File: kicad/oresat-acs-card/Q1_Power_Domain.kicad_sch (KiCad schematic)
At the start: 69 parts, among them Q11 MOSFET-PCH-SOT23-6, Q12 MOSFET-PCH-SOT23-6, Q13 PMV45EN2R, Q14 PMV45EN2R, Q15 MOSFET-PCH-dual-SOT23-6, U10 MAX4211FETE, U11 MIC842LYC5-TR, U12 MIC842LYC5-TR, U9 MAX7310ATE

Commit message: Updated ACS board. Changed mezzanine pinouts. Added 5 V supplies for each quadrant. Updated layout.
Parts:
- added C20: 10u, oresat-acs-card:.0805-B-NOSILK, symbol Device:C_Small
- added C57: 1u, Resistor_SMD:R_0603_1608Metric, symbol Device:C_Small
- added C64: 22u, Capacitor_SMD:C_1210_3225Metric, symbol Device:C_Small
- added C84: CL10B104KB8NNNL, oresat-acs-card:.0603-C-NOSILK, symbol oresat-acs-card-eagle-import:C-EU0603-C-NOSILK
- added D1: 150060VS55040, oresat-acs-card:LED-0603, symbol oresat-live-card-eagle-import:LED-GREEN0603
- added L1: 6.8u, oresat-acs-card:ECS-MPI4040, symbol oresat-live-card-eagle-import:L-ECS-MPI4040
- added R116, R117: RC0603FR-0710KL, oresat-acs-card:.0603-C-NOSILK, symbol oresat-acs-card-eagle-import:R-US_0603-C-NOSILK
- added R14, R26: 10k, Resistor_SMD:R_0603_1608Metric, symbol oresat-live-card-eagle-import:R-US_0603-A
- added TP51: TEST-POINT-LARGE-SQUARE, oresat-acs-card:1X01, symbol oresat-acs-card-eagle-import:TEST-POINT-LARGE-SQUARE
- added U24: TPS62112, oresat-acs-card:S-PVQFN-16, symbol oresat-live-card-eagle-import:TPS6211X
- added U38: TS5A21366DCUR, oresat-acs-card:DCU-R-PDSO-G8, symbol oresat-acs-card-eagle-import:TS5A21366DCUR
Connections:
- net GND: now also C20.2, C57.2, C64.2, C84.1, D1.C, U24.1 (GND), U24.11 (GND), U24.12 (GND), U24.16 (GND), U24.6 (LBO), U24.7 (LBI), U24.9 (GND), U24.PAD (GND), U38.4 (GND)
- net VBUSP_Q1: now also C20.1, C57.1, R14.2, U24.2 (VIN), U24.3 (VIN), U24.4 (EN), U24.8 (VIN)
- net VPD_Q1: now also C84.2, U38.8 (VCC)
- net at TP39.1, U9.12 (IO7): now also U38.3 (IN2), U38.7 (IN1)
- new net: D1.A, R26.1
- new net: R116.2, U38.1 (NO1)
- new net: R117.2, U38.5 (NO2)
- new net: R14.1, U24.5 (SYNC)
- new net: L1.1, U24.14 (SW), U24.15 (SW)
- new net 5V_Q1: C64.1, L1.2, R26.2, TP51.1, U24.10 (FB)
- new net C3-UART-RX: R116.1
- new net C3-UART-TX: R117.1
- new net UART_RX_Q1: U38.6 (COM2)
- new net UART_TX_Q1: U38.2 (COM1)
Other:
- note added: "0805"
- note added: "5V Card Switching Supply"

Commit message: Updated 5 V regulator and tweaked card layout. Cleaned up silkscreen layer and schematic.
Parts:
- removed L1: 6.8u, oresat-acs-card:ECS-MPI4040, symbol oresat-live-card-eagle-import:L-ECS-MPI4040
- removed R14, R26: 10k, Resistor_SMD:R_0603_1608Metric, symbol oresat-live-card-eagle-import:R-US_0603-A
- removed U24: TPS62112, oresat-acs-card:S-PVQFN-16, symbol oresat-live-card-eagle-import:TPS6211X
- added L1: 3u3, Inductor_SMD:L_Coilcraft_XxL4030, symbol Device:L_Small
- added R14, R19, R26: 100k, Resistor_SMD:R_0603_1608Metric, symbol Device:R_Small_US
- added U24: LTC3624, Package_DFN_QFN:DFN-8-1EP_3x3mm_P0.5mm_EP1.65x2.38mm, symbol U-Linear Tech-LTC3624:LTC3624
- C20: footprint oresat-acs-card:.0805-B-NOSILK -> Capacitor_SMD:C_0805_2012Metric; Distributor DigiKey -> (none); MPN CGA4J1X7R0J106M125AC -> (none)
- C57: value 1u -> 2u2; footprint Resistor_SMD:R_0603_1608Metric -> Capacitor_SMD:C_0603_1608Metric; Distributor DigiKey -> (none); MPN CGA3E1X7R1E105M080AE -> (none)
- C64: value 22u -> 47u; footprint Capacitor_SMD:C_1210_3225Metric -> Capacitor_SMD:C_1206_3216Metric; Distributor DigiKey -> (none); MFR (none) -> KYOCERA AVX; MPN CGA6P1X7R1C226M250AC -> 1206YD476MAT2A
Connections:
- net 5V_Q1: now also L1.2, R26.1, U24.5 (FB)
- net GND: now also R19.2, U24.8 (GND), U24.9 (GND)
- net VBUSP_Q1: now also U24.2 (Vin), U24.3 (RUN); no longer C57.1
- net at D1.A: now also R26.2
- new net: C57.1, R14.2, U24.6 (INTVcc)
- new net: L1.1, U24.1 (SW)
- new net: R14.1, R19.1, U24.7 (MODE)
- no-connect marks 0 -> 1
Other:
- note removed: "0805"
- moved on the sheet: C11, C12, C13, C14, C15, C84, D1, D5, D6, Q11A, Q12A, Q13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

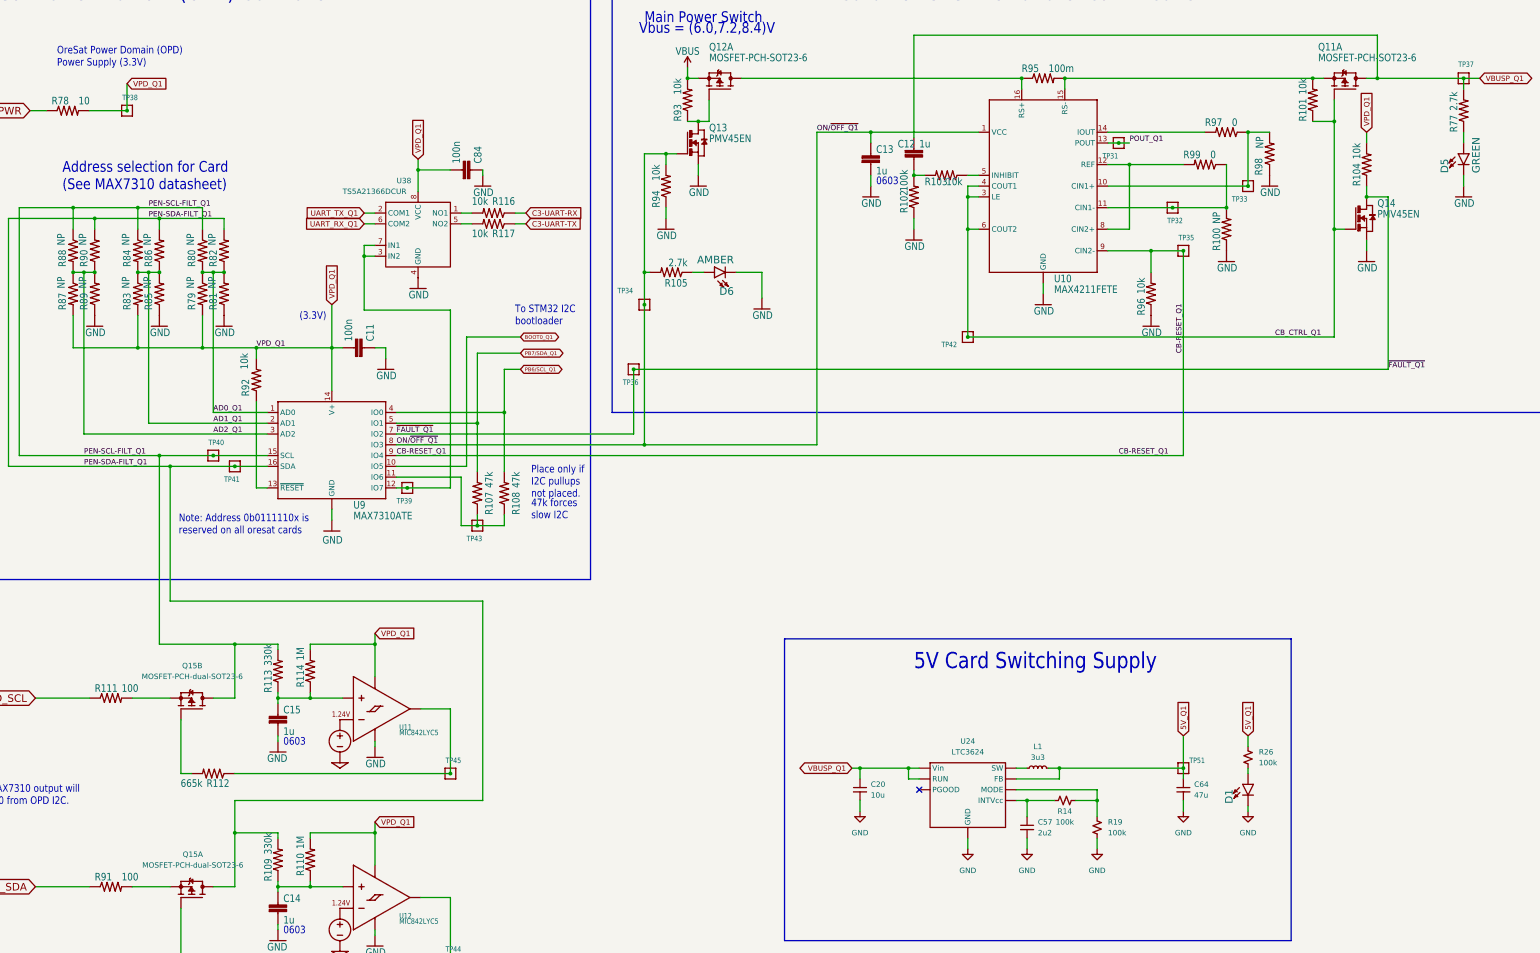
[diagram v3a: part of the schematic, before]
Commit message: Updated 5V regulators to match design block. Added UART switch to microcontroller. Added power flags and cleaned up ERC errors
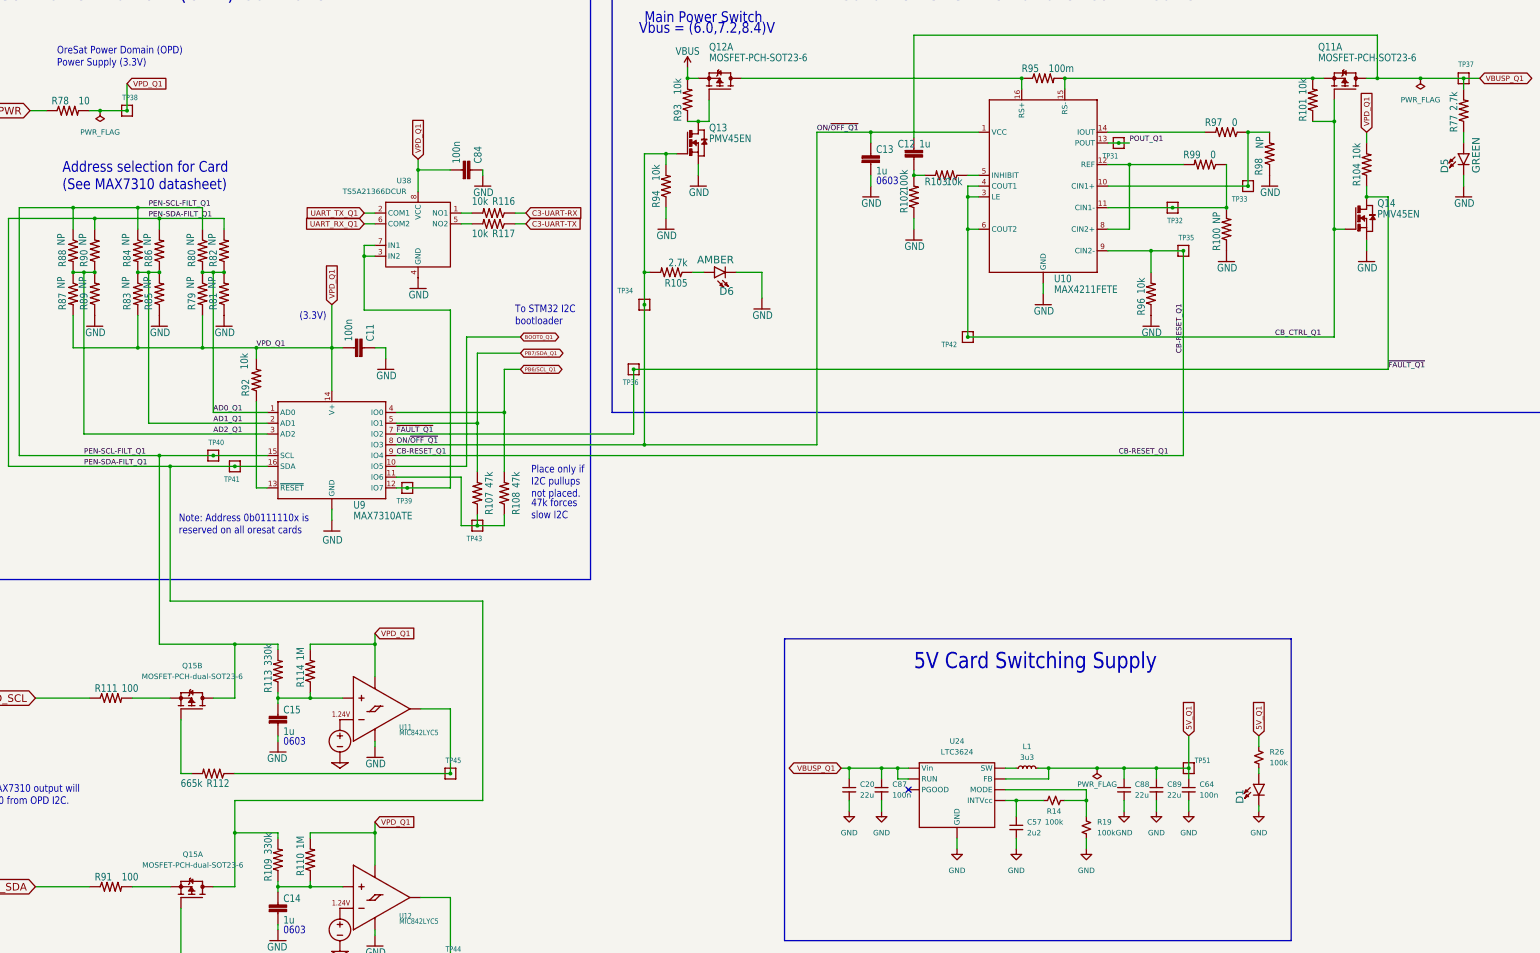
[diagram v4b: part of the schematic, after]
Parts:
- added C87: 100n, Capacitor_SMD:C_0603_1608Metric, symbol Device:C_Small
- added C88, C89: 22u, Capacitor_SMD:C_1210_3225Metric, symbol Device:C_Small
- C20: value 10u -> 22u; footprint Capacitor_SMD:C_0805_2012Metric -> Capacitor_SMD:C_1210_3225Metric
- C64: value 47u -> 100n; footprint Capacitor_SMD:C_1206_3216Metric -> Capacitor_SMD:C_0603_1608Metric
- D1: value 150060VS55040 -> LED-GREEN0603; symbol oresat-live-card-eagle-import:LED-GREEN0603 -> oresat-acs-card-eagle-import:LED-GREEN0603
- L1: footprint Inductor_SMD:L_Coilcraft_XxL4030 -> oresat-footprints:L_ECS-MPI4040
- U24: footprint Package_DFN_QFN:DFN-8-1EP_3x3mm_P0.5mm_EP1.65x2.38mm -> oresat-footprints:DFN-8-1EP_3x3mm_P0.5mm_EP1.65x2.38mm_ThermalVias0.3mm
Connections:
- net 5V_Q1: now also C88.1, C89.1
- net GND: now also C87.2, C88.2, C89.2
- net VBUSP_Q1: now also C87.1
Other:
- moved on the sheet: C20, C57, C64, D1, L1, R14, R19, R26, TP51, U24

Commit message: Design review changes.
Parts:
- R26: value 100k -> 10k
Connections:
- net VPD_Q1: no longer C84.2, U38.8 (VCC)
- net ON/~{OFF_Q1} renamed ON/~{OFF}_Q1
- net ON/~{OFF}_Q1: now also C84.2, U38.8 (VCC)
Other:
- note added: "Resistor values TBD"
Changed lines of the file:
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@@
   (junction (at 58.42 67.31) (diameter 0) (color 0 0 0 0)
+  )
+  (junction (at 193.04 54.61) (diameter 0) (color 0 0 0 0)
   )
   (junction (at 78.74 82.55) (diameter 0) (color 0 0 0 0)
@@
     (stroke (width 0) (type default) (color 0 0 0 0))
   )
+  (wire (pts (xy 193.04 54.61) (xy 139.7 54.61))
+    (stroke (width 0) (type default) (color 0 0 0 0))
+  )
   (wire (pts (xy 83.82 200.66) (xy 83.82 187.96))
     (stroke (width 0) (type default) (color 0 0 0 0))
@@
     (stroke (width 0) (type default) (color 0 0 0 0))
   )
-  (wire (pts (xy 139.7 55.88) (xy 139.7 58.42))
+  (wire (pts (xy 139.7 54.61) (xy 139.7 58.42))
     (stroke (width 0) (type default) (color 0 0 0 0))
   )
@@
     (effects (font (size 1.778 1.5113)) (justify left bottom))
   )
+  (text "Resistor values TBD" (at 304.8 45.72 0)
+    (effects (font (size 1.27 1.27)) (justify left bottom))
+  )
   (text "47k forces\nslow I2C" (at 166.37 140.97 180)
     (effects (font (size 1.778 1.5113)) (justify left bottom))
@@
     (effects (font (size 3.81 3.2385)) (justify left bottom))
   )
-  (label "ON/~{OFF_Q1}" (at 134.62 123.19 0)
+  (label "ON{slash}~{OFF}_Q1" (at 134.62 123.19 0)
     (effects (font (size 1.2446 1.2446)) (justify left bottom))
   )
@@
     (effects (font (size 1.2446 1.2446)) (justify left bottom))
   )
+  (label "ON/~{OFF}_Q1" (at 139.7 54.61 0)
+    (effects (font (size 1.2446 1.2446)) (justify left bottom))
+  )
   (label "CB-RESET_Q1" (at 134.62 125.73 0)
     (effects (font (size 1.2446 1.2446)) (justify left bottom))
@@
     (effects (font (size 1.2446 1.2446)) (justify left bottom))
   )
-  (label "ON/~{OFF_Q1}" (at 233.68 49.53 0)
+  (label "ON/~{OFF}_Q1" (at 233.68 49.53 0)
     (effects (font (size 1.2446 1.2446)) (justify left bottom))
   )
@@
   )
   (label "AD2_Q1" (at 91.44 120.65 0)
+    (effects (font (size 1.2446 1.2446)) (justify left bottom))
+  )
+  (label "ON/~{OFF}_Q1" (at 193.04 68.58 90)
     (effects (font (size 1.2446 1.2446)) (justify left bottom))
   )
@@
     (effects (font (size 1.27 1.27)) (justify left))
     (property "Intersheet References" "${INTERSHEET_REFS}" (id 0) (at 139.0893 167.5606 0)
-      (effects (font (size 1.27 1.27)) (justify left) hide)
-    )
-  )
-  (global_label "VPD_Q1" (shape input) (at 139.7 55.88 90) (fields_autoplaced)
-    (effects (font (size 1.27 1.27)) (justify left))
-    (property "Intersheet References" "${INTERSHEET_REFS}" (id 0) (at 139.6206 46.3307 90)
       (effects (font (size 1.27 1.27)) (justify left) hide)
     )
@@
       (effects (font (size 1.27 1.27)) (justify left))
     )
-    (property "Value" "100k" (id 1) (at 340.36 198.1199 0)
+    (property "Value" "10k" (id 1) (at 340.36 198.1199 0)
       (effects (font (size 1.27 1.27)) (justify left))
     )
@@
       (effects (font (size 1.778 1.5113)) (justify left bottom))
     )
-    (property "Value" "2.7k" (id 1) (at 203.2 79.248 0)
+    (property "Value" "4.7k" (id 1) (at 203.2 79.248 0)
       (effects (font (size 1.778 1.5113)) (justify left bottom))
     )
@@
       (effects (font (size 1.778 1.5113)) (justify left bottom))
     )
-    (property "Value" "2.7k" (id 1) (at 384.81 44.45 0)
+    (property "Value" "10k" (id 1) (at 384.81 44.45 0)
       (effects (font (size 1.778 1.5113)) (justify left bottom))
     )
@@
   (symbol (lib_id "oresat-acs-card-eagle-import:C-EU0603-C-NOSILK") (at 152.4 58.42 270) (mirror x) (unit 1)
     (in_bom yes) (on_board yes)
-    (property "Reference" "C84" (id 0) (at 152.781 56.896 0)
-      (effects (font (size 1.778 1.5113)) (justify left bottom))
-    )
-    (property "Value" "100n" (id 1) (at 147.701 56.896 0)
-      (effects (font (size 1.778 1.5113)) (justify left bottom))
-    )
+    (property "Reference" "C84" (id 0) (at 152.4 55.245 90)
+      (effects (font (size 1.778 1.5113)) (justify left bottom))
+    )
+    (property "Value" "100n" (id 1) (at 144.145 55.245 90)
+      (effects (font (size 1.778 1.5113)) (justify left bottom))
+    )
